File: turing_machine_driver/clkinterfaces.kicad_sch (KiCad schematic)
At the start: 24 parts, among them J2 Header Position Value, J3 Symbol Register Value, J4 State Register Value, J5 External Interface, U1 74LS14, U2 74LS03, U7 NE555P, U8 NE555P

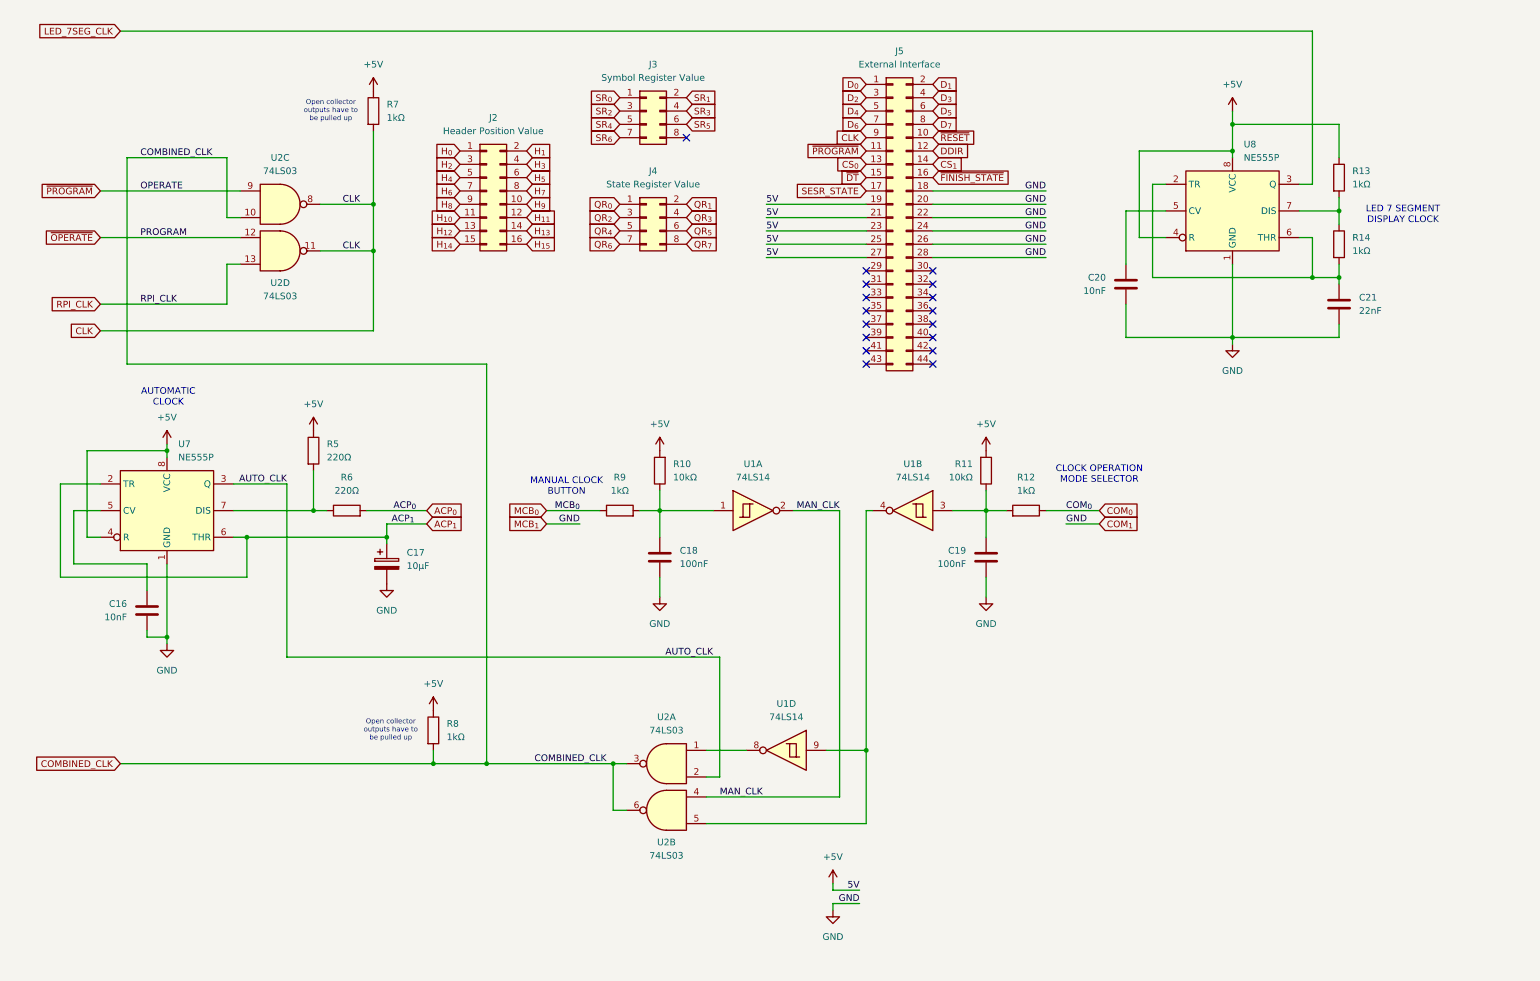
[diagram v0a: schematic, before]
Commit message: added control panel and moved LEDs to it
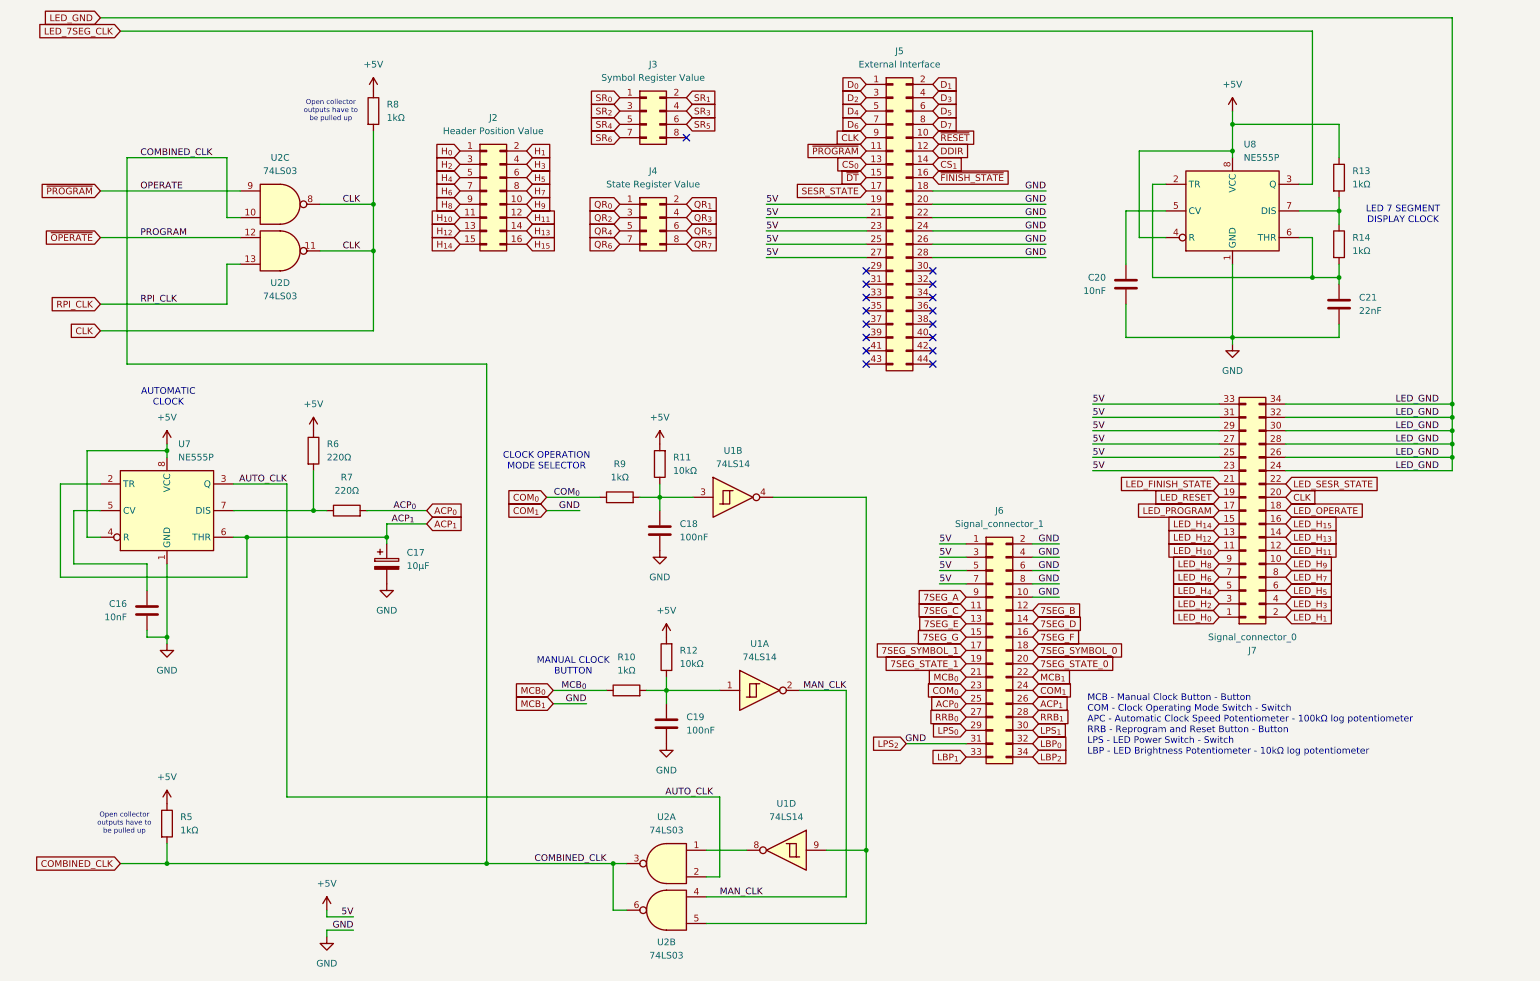
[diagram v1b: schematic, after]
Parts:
- added J6: Signal_connector_1, Connector_Edge:Connector_Edge_2x17pin_odd, symbol Connector_Generic:Conn_02x17_Odd_Even
- added J7: Signal_connector_0, Connector_Edge:Connector_Edge_2x17pin_odd, symbol Connector_Generic:Conn_02x17_Odd_Even
- renumbered C19 to C18, C18 to C19, R9 to R10, R10 to R12, R8 to R5, R5 to R6, R6 to R7, R7 to R8, R12 to R9
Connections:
- net +5V: now also J6.1 (Pin_1), J6.3 (Pin_3), J6.5 (Pin_5), J6.7 (Pin_7), J7.23 (Pin_23), J7.25 (Pin_25), J7.27 (Pin_27), J7.29 (Pin_29), J7.31 (Pin_31), J7.33 (Pin_33)
- net ACP_{0}: now also J6.25 (Pin_25)
- net ACP_{1}: now also J6.26 (Pin_26)
- net CLK: now also J7.20 (Pin_20)
- net COM_{0}: now also J6.23 (Pin_23)
- net GND: now also J6.10 (Pin_10), J6.2 (Pin_2), J6.22 (Pin_22), J6.24 (Pin_24), J6.31 (Pin_31), J6.4 (Pin_4), J6.6 (Pin_6), J6.8 (Pin_8)
- net MCB_{0}: now also J6.21 (Pin_21)
- new net 7SEG_A: J6.9 (Pin_9)
- new net 7SEG_B: J6.12 (Pin_12)
- new net 7SEG_C: J6.11 (Pin_11)
- new net 7SEG_D: J6.14 (Pin_14)
- new net 7SEG_E: J6.13 (Pin_13)
- new net 7SEG_F: J6.16 (Pin_16)
- new net 7SEG_G: J6.15 (Pin_15)
- new net 7SEG_STATE_0: J6.20 (Pin_20)
- new net 7SEG_STATE_1: J6.19 (Pin_19)
- new net 7SEG_SYMBOL_0: J6.18 (Pin_18)
- new net 7SEG_SYMBOL_1: J6.17 (Pin_17)
- new net LBP_{0}: J6.32 (Pin_32)
- new net LBP_{1}: J6.33 (Pin_33)
- new net LBP_{2}: J6.34 (Pin_34)
- new net LED_FINISH_STATE: J7.21 (Pin_21)
- new net LED_GND: J7.24 (Pin_24), J7.26 (Pin_26), J7.28 (Pin_28), J7.30 (Pin_30), J7.32 (Pin_32), J7.34 (Pin_34)
- new net LED_H_{0}: J7.1 (Pin_1)
- new net LED_H_{10}: J7.11 (Pin_11)
- new net LED_H_{11}: J7.12 (Pin_12)
- new net LED_H_{12}: J7.13 (Pin_13)
- new net LED_H_{13}: J7.14 (Pin_14)
- new net LED_H_{14}: J7.15 (Pin_15)
- new net LED_H_{15}: J7.16 (Pin_16)
- new net LED_H_{1}: J7.2 (Pin_2)
- new net LED_H_{2}: J7.3 (Pin_3)
- new net LED_H_{3}: J7.4 (Pin_4)
- new net LED_H_{4}: J7.5 (Pin_5)
- new net LED_H_{5}: J7.6 (Pin_6)
- new net LED_H_{6}: J7.7 (Pin_7)
- new net LED_H_{7}: J7.8 (Pin_8)
- new net LED_H_{8}: J7.9 (Pin_9)
- new net LED_H_{9}: J7.10 (Pin_10)
- new net LED_OPERATE: J7.18 (Pin_18)
- new net LED_PROGRAM: J7.17 (Pin_17)
- new net LED_RESET: J7.19 (Pin_19)
- new net LED_SESR_STATE: J7.22 (Pin_22)
- new net LPS_{0}: J6.29 (Pin_29)
- new net LPS_{1}: J6.30 (Pin_30)
- new net RRB_{0}: J6.27 (Pin_27)
- new net RRB_{1}: J6.28 (Pin_28)
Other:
- note added: "MCB - Manual Clock Button - Button COM - Clock Operating Mode Switch - Switch APC - Automatic Clock Speed Potentiometer - 100kΩ log potentiometer RRB - Reprogram and Reset Button - Button LPS - LED Power Switch - Switch LBP - LED Brightness Potentiometer - 10kΩ log potentiometer"
- moved on the sheet: C18, C19, R10, R11, R12, R5, R9, U1A, U1B, U1D, U2A, U2B

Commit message: finished driver PCB layout
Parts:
- renumbered C16 to C19, C17 to C20, C18 to C21, C19 to C22, C20 to C23, C21 to C24
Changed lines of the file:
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@@
 		(dnp no)
 		(fields_autoplaced yes)
-		(property "Reference" "#PWR049"
+		(property "Reference" "#PWR055"
 			(at 66.04 97.79 0)
 			(effects
@@
 			(project "turing_driver"
 				(path "/c2889866-f59b-4a7d-9ec7-f6fbf53024cb/14de9027-98ad-494f-868a-ee5ecea16656"
-					(reference "#PWR049")
+					(reference "#PWR055")
 					(unit 1)
 				)
@@
 		(dnp no)
 		(fields_autoplaced yes)
-		(property "Reference" "#PWR046"
+		(property "Reference" "#PWR052"
 			(at 38.1 100.33 0)
 			(effects
@@
 			(project "turing_driver"
 				(path "/c2889866-f59b-4a7d-9ec7-f6fbf53024cb/14de9027-98ad-494f-868a-ee5ecea16656"
-					(reference "#PWR046")
+					(reference "#PWR052")
 					(unit 1)
 				)
@@
 		(dnp no)
 		(fields_autoplaced yes)
-		(property "Reference" "C19"
+		(property "Reference" "C22"
 			(at 137.16 148.5899 0)
 			(effects
@@
 			(project "turing_driver"
 				(path "/c2889866-f59b-4a7d-9ec7-f6fbf53024cb/14de9027-98ad-494f-868a-ee5ecea16656"
-					(reference "C19")
+					(reference "C22")
 					(unit 1)
 				)
@@
 		(dnp no)
 		(fields_autoplaced yes)
-		(property "Reference" "#PWR058"
+		(property "Reference" "#PWR064"
 			(at 241.3 36.83 0)
 			(effects
@@
 			(project "turing_driver"
 				(path "/c2889866-f59b-4a7d-9ec7-f6fbf53024cb/14de9027-98ad-494f-868a-ee5ecea16656"
-					(reference "#PWR058")
+					(reference "#PWR064")
 					(unit 1)
 				)
@@
 		(on_board yes)
 		(dnp no)
-		(property "Reference" "C21"
+		(property "Reference" "C24"
 			(at 265.43 68.5799 0)
 			(effects
@@
 			(project "turing_driver"
 				(path "/c2889866-f59b-4a7d-9ec7-f6fbf53024cb/14de9027-98ad-494f-868a-ee5ecea16656"
-					(reference "C21")
+					(reference "C24")
 					(unit 1)
 				)
@@
 		(dnp no)
 		(fields_autoplaced yes)
-		(property "Reference" "#PWR050"
+		(property "Reference" "#PWR056"
 			(at 68.58 189.23 0)
 			(effects
@@
 			(project "turing_driver"
 				(path "/c2889866-f59b-4a7d-9ec7-f6fbf53024cb/14de9027-98ad-494f-868a-ee5ecea16656"
-					(reference "#PWR050")
+					(reference "#PWR056")
 					(unit 1)
 				)
@@
 		(dnp no)
 		(fields_autoplaced yes)
-		(property "Reference" "#PWR054"
+		(property "Reference" "#PWR060"
 			(at 132.08 100.33 0)
 			(effects
@@
 			(project "turing_driver"
 				(path "/c2889866-f59b-4a7d-9ec7-f6fbf53024cb/14de9027-98ad-494f-868a-ee5ecea16656"
-					(reference "#PWR054")
+					(reference "#PWR060")
 					(unit 1)
 				)
@@
 		(dnp no)
 		(fields_autoplaced yes)
-		(property "Reference" "#PWR053"
+		(property "Reference" "#PWR059"
 			(at 80.01 129.54 0)
 			(effects
@@
 			(project "turing_driver"
 				(path "/c2889866-f59b-4a7d-9ec7-f6fbf53024cb/14de9027-98ad-494f-868a-ee5ecea16656"
-					(reference "#PWR053")
+					(reference "#PWR059")
 					(unit 1)
 				)
@@
 		(on_board yes)
 		(dnp no)
-		(property "Reference" "C20"
+		(property "Reference" "C23"
 			(at 217.17 64.7699 0)
 			(effects
@@
 			(project "turing_driver"
 				(path "/c2889866-f59b-4a7d-9ec7-f6fbf53024cb/14de9027-98ad-494f-868a-ee5ecea16656"
-					(reference "C20")
+					(reference "C23")
 					(unit 1)
 				)
@@
 		(dnp no)
 		(fields_autoplaced yes)
-		(property "Reference" "#PWR055"
+		(property "Reference" "#PWR061"
 			(at 132.08 123.19 0)
 			(effects
@@
 			(project "turing_driver"
 				(path "/c2889866-f59b-4a7d-9ec7-f6fbf53024cb/14de9027-98ad-494f-868a-ee5ecea16656"
-					(reference "#PWR055")
+					(reference "#PWR061")
 					(unit 1)
 				)
@@
 		(dnp no)
 		(fields_autoplaced yes)
-		(property "Reference" "C17"
+		(property "Reference" "C20"
 			(at 83.82 117.2209 0)
 			(effects
@@
 			(project "turing_driver"
 				(path "/c2889866-f59b-4a7d-9ec7-f6fbf53024cb/14de9027-98ad-494f-868a-ee5ecea16656"
-					(reference "C17")
+					(reference "C20")
 					(unit 1)
 				)
@@
 		(dnp no)
 		(fields_autoplaced yes)
-		(property "Reference" "#PWR051"
+		(property "Reference" "#PWR057"
 			(at 68.58 196.85 0)
 			(effects
@@
 			(project "turing_driver"
 				(path "/c2889866-f59b-4a7d-9ec7-f6fbf53024cb/14de9027-98ad-494f-868a-ee5ecea16656"
-					(reference "#PWR051")
+					(reference "#PWR057")
 					(unit 1)
 				)
@@
 		(dnp no)
 		(fields_autoplaced yes)
-		(property "Reference" "#PWR048"
+		(property "Reference" "#PWR054"
 			(at 38.1 168.91 0)
 			(effects
@@
 			(project "turing_driver"
 				(path "/c2889866-f59b-4a7d-9ec7-f6fbf53024cb/14de9027-98ad-494f-868a-ee5ecea16656"
-					(reference "#PWR048")
+					(reference "#PWR054")
 					(unit 1)
 				)
@@
 		(on_board yes)
 		(dnp no)
-		(property "Reference" "C16"
+		(property "Reference" "C19"
 			(at 30.48 126.9999 0)
 			(effects
@@
 			(project "turing_driver"
 				(path "/c2889866-f59b-4a7d-9ec7-f6fbf53024cb/14de9027-98ad-494f-868a-ee5ecea16656"
-					(reference "C16")
+					(reference "C19")
 					(unit 1)
 				)
@@
 		(dnp no)
 		(fields_autoplaced yes)
-		(property "Reference" "#PWR057"
+		(property "Reference" "#PWR063"
 			(at 133.35 160.02 0)
 			(effects
@@
 			(project "turing_driver"
 				(path "/c2889866-f59b-4a7d-9ec7-f6fbf53024cb/14de9027-98ad-494f-868a-ee5ecea16656"
-					(reference "#PWR057")
+					(reference "#PWR063")
 					(unit 1)
 				)
@@
 		(dnp no)
 		(fields_autoplaced yes)
-		(property "Reference" "#PWR047"
+		(property "Reference" "#PWR053"
 			(at 38.1 140.97 0)
 			(effects
@@
 			(project "turing_driver"
 				(path "/c2889866-f59b-4a7d-9ec7-f6fbf53024cb/14de9027-98ad-494f-868a-ee5ecea16656"
-					(reference "#PWR047")
+					(reference "#PWR053")
 					(unit 1)
 				)
@@
 		(dnp no)
 		(fields_autoplaced yes)
-		(property "Reference" "#PWR052"
+		(property "Reference" "#PWR058"
 			(at 77.47 33.02 0)
 			(effects
@@
 			(project "turing_driver"
 				(path "/c2889866-f59b-4a7d-9ec7-f6fbf53024cb/14de9027-98ad-494f-868a-ee5ecea16656"
-					(reference "#PWR052")
+					(reference "#PWR058")
 					(unit 1)
 				)
@@
 		(dnp no)
 		(fields_autoplaced yes)
-		(property "Reference" "#PWR059"
+		(property "Reference" "#PWR065"
 			(at 241.3 83.82 0)
 			(effects
@@
 			(project "turing_driver"
 				(path "/c2889866-f59b-4a7d-9ec7-f6fbf53024cb/14de9027-98ad-494f-868a-ee5ecea16656"
-					(reference "#PWR059")
+					(reference "#PWR065")
 					(unit 1)
 				)
@@
 		(dnp no)
 		(fields_autoplaced yes)
-		(property "Reference" "C18"
+		(property "Reference" "C21"
 			(at 135.89 111.7599 0)
 			(effects
@@
 			(project "turing_driver"
 				(path "/c2889866-f59b-4a7d-9ec7-f6fbf53024cb/14de9027-98ad-494f-868a-ee5ecea16656"
-					(reference "C18")
+					(reference "C21")
 					(unit 1)
 				)
@@
 		(dnp no)
 		(fields_autoplaced yes)
-		(property "Reference" "#PWR056"
+		(property "Reference" "#PWR062"
 			(at 133.35 137.16 0)
 			(effects
@@
 			(project "turing_driver"
 				(path "/c2889866-f59b-4a7d-9ec7-f6fbf53024cb/14de9027-98ad-494f-868a-ee5ecea16656"
-					(reference "#PWR056")
+					(reference "#PWR062")
 					(unit 1)
 				)
